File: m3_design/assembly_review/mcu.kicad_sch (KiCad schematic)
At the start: 18 parts, among them J2 SWD+DFU 1x6, U1 STM32H743VIT6, Y1 25MHz CL8pF

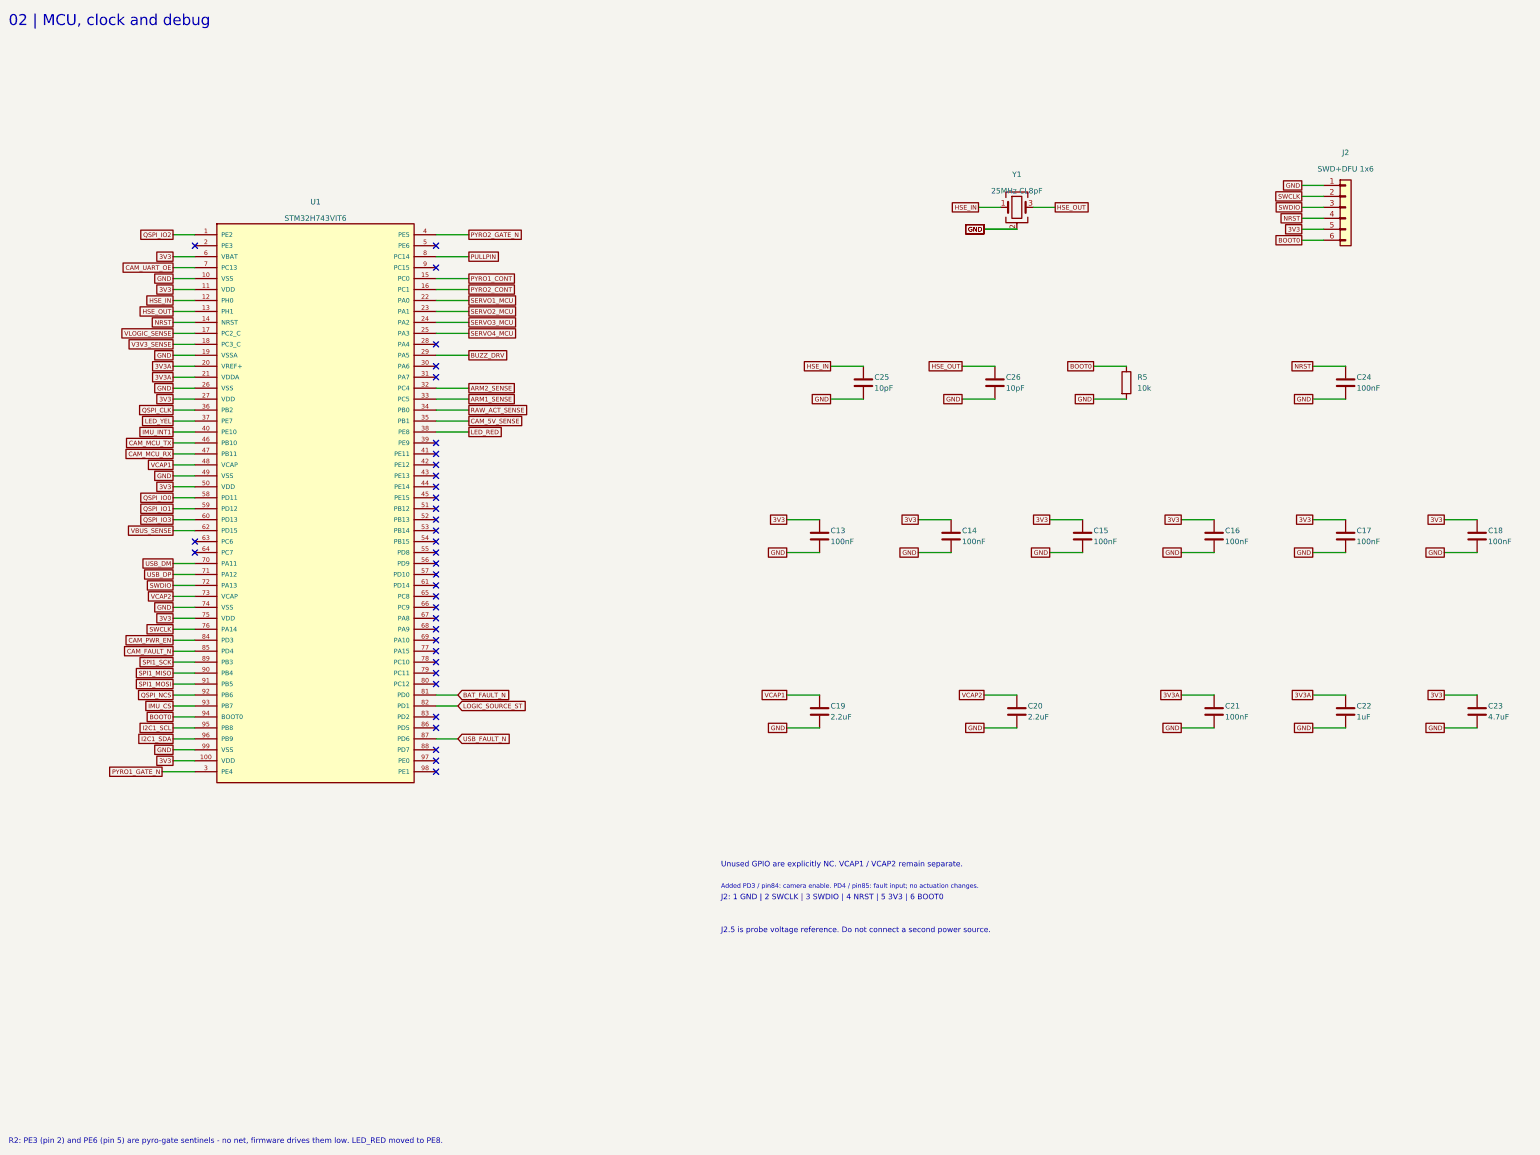
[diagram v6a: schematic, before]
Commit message: M3-ASSY-R4: R3 validation fixes, new IMU, fault-tolerant pyro sensing
The board, schematic sheets and footprint library are generated from
R3 (533af8e) by m3_design/r4_build.sh (r4_lib.py, r4_sch.py,
r4_pcb.py). docs/REQUIREMENTS.md states what the board must do;
docs/M3_R4.md records every change, the thirteen evaluation passes
(twelve independent reviews) and the accepted deviations.

- IMU: ST LSM6DSV320X (16 g and 320 g, 4000 dps)
- Pyro: black ARM and orange igniter terminals, eight pyro spacing
  rules in m3.kicad_dru, sense dividers of 2 x 5.1k over 2 x 2k in
  parallel, 4.7k at each ADC pin (R168-R172)
- Pull-pin on a JST PH connector; JLC tooling holes
- Fab: Standard PCBA, 84 BOM lines, 205 placed parts, $80.12 per board
  at five boards (tools/jlc_cost.py); placement rotations verified
- Gate: tools/check.sh DRC 0, unconnected 0, schematic parity 0, ERC 0,
  audit OK; m3_design/check_actuators.py OK

Nothing has been built or measured, and there is no R4 firmware. The
open owner decisions and the bench tests are listed in STATUS.md.

Co-Authored-By: Claude Opus 5.5 <noreply@anthropic.com>
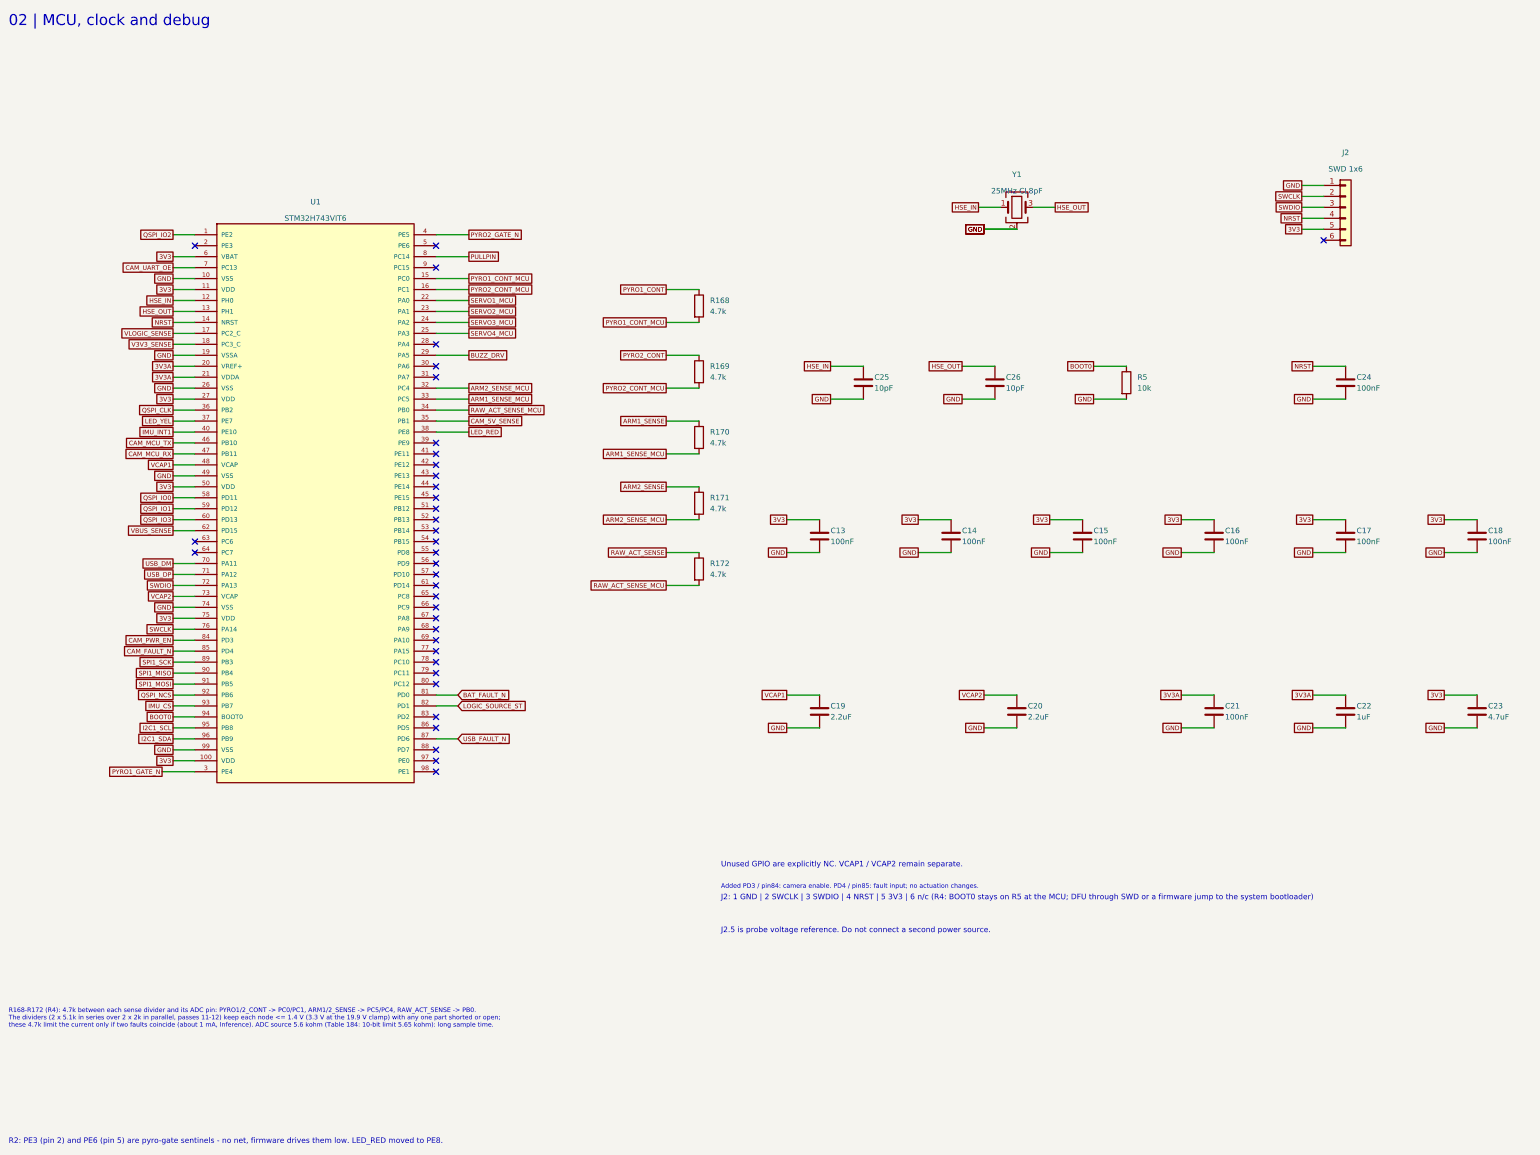
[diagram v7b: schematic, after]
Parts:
- added R168, R169, R170, R171, R172: 4.7k, rocket:R0402, symbol M3:R
- J2: value SWD+DFU 1x6 -> SWD 1x6
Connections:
- net ARM1_SENSE: now also R170.1; no longer U1.33 (PC5)
- net ARM2_SENSE: now also R171.1; no longer U1.32 (PC4)
- net BOOT0: no longer J2.6 (Pin_6)
- net PYRO1_CONT: now also R168.1; no longer U1.15 (PC0)
- net PYRO2_CONT: now also R169.1; no longer U1.16 (PC1)
- net RAW_ACT_SENSE: now also R172.1; no longer U1.34 (PB0)
- new net ARM1_SENSE_MCU: R170.2, U1.33 (PC5)
- new net ARM2_SENSE_MCU: R171.2, U1.32 (PC4)
- new net PYRO1_CONT_MCU: R168.2, U1.15 (PC0)
- new net PYRO2_CONT_MCU: R169.2, U1.16 (PC1)
- new net RAW_ACT_SENSE_MCU: R172.2, U1.34 (PB0)
- no-connect marks 36 -> 37
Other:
- note added: "J2: 1 GND | 2 SWCLK | 3 SWDIO | 4 NRST | 5 3V3 | 6 n/c (R4: BOOT0 stays on R5 at the MCU; DFU through SWD or a firmware jump to the system bootloader)"
- note added: "R168-R172 (R4): 4.7k between each sense divider and its ADC pin: PYRO1/2_CONT -> PC0/PC1, ARM1/2_SENSE -> PC5/PC4, RAW_ACT_SENSE -> PB0. The dividers (2 x 5.1k in series over 2 x 2k in parallel, passes 11-12) keep each node <= 1.4 V (3.3 V at the 19.9 V clamp) with any one part shorted or open; these 4.7k limit the current only if two faults coincide (about 1 mA, Inference). ADC source 5.6 kohm (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"
- note removed: "J2: 1 GND | 2 SWCLK | 3 SWDIO | 4 NRST | 5 3V3 | 6 BOOT0"
